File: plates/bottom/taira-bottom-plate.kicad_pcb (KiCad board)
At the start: 2 copper layers, 151.5 x 121.2 mm, 8 parts

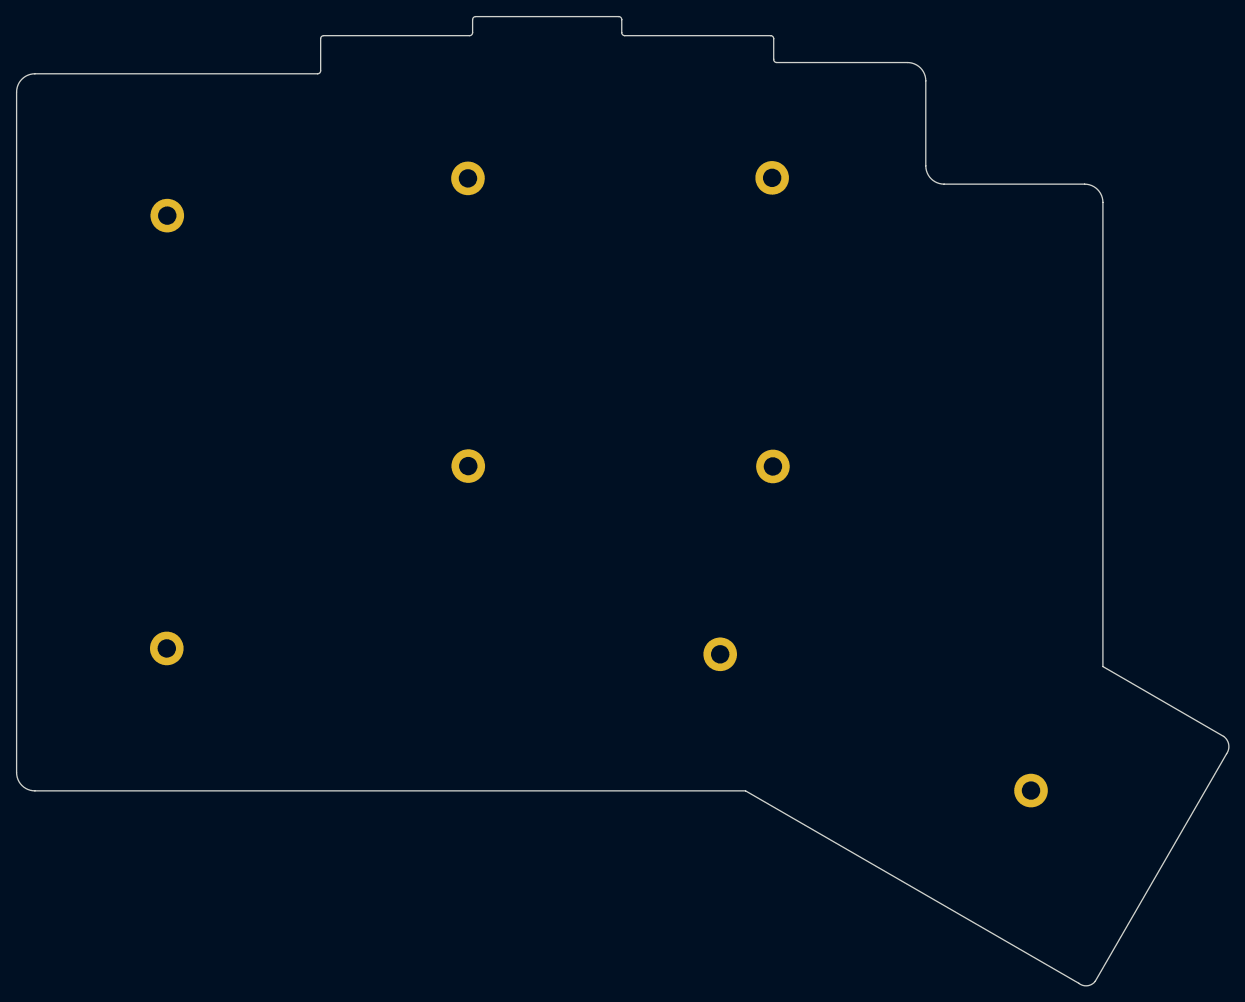
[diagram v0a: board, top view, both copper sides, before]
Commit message: kicad 4 -> 10
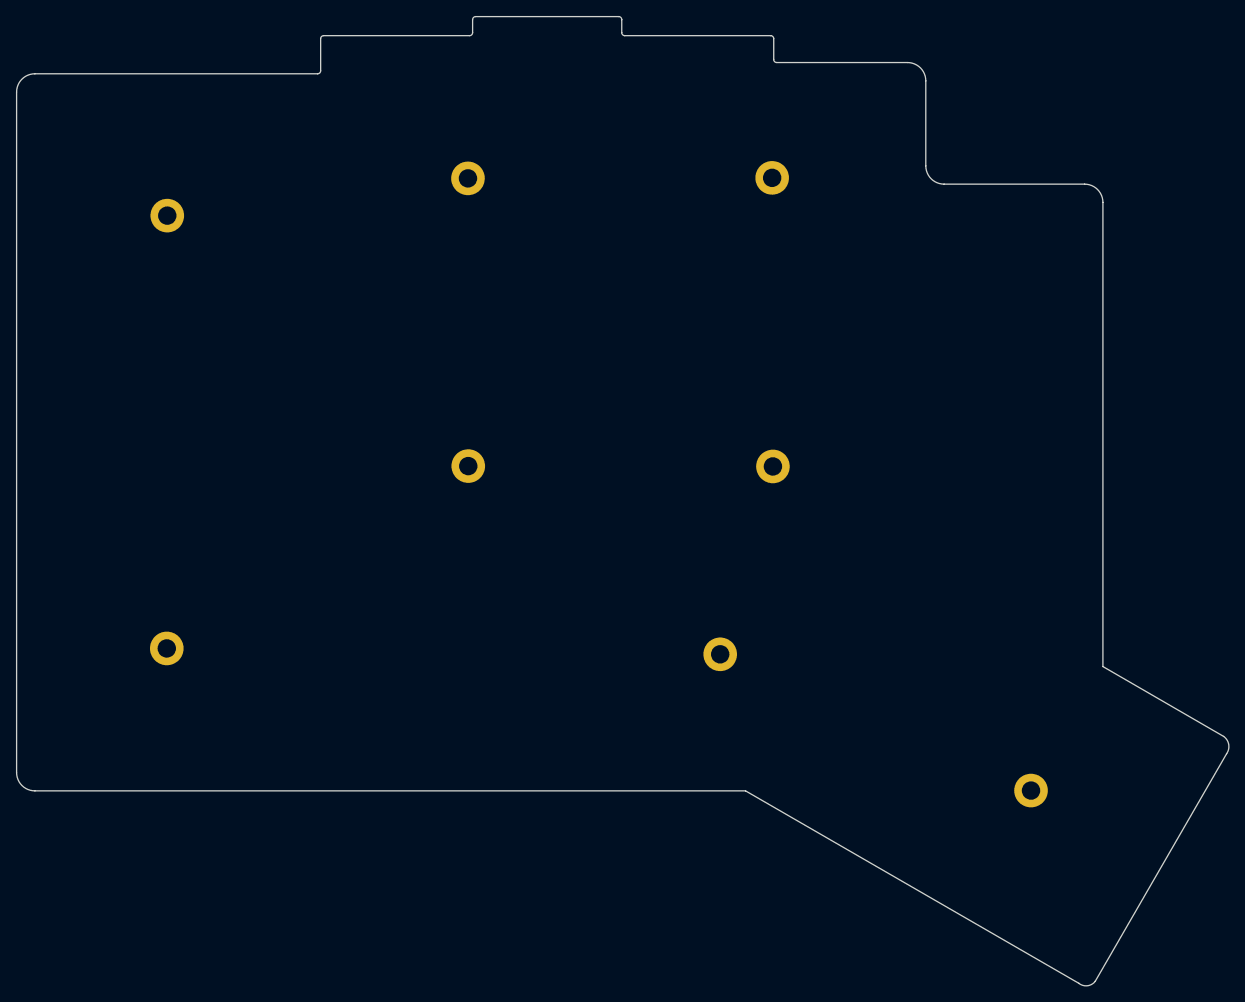
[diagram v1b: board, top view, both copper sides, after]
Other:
- net class Default removed
